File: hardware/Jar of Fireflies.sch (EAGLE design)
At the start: 31 parts, among them IC1 ATTINY85, J1 PJ-006A, J3 SENSOR, J4 ICSP

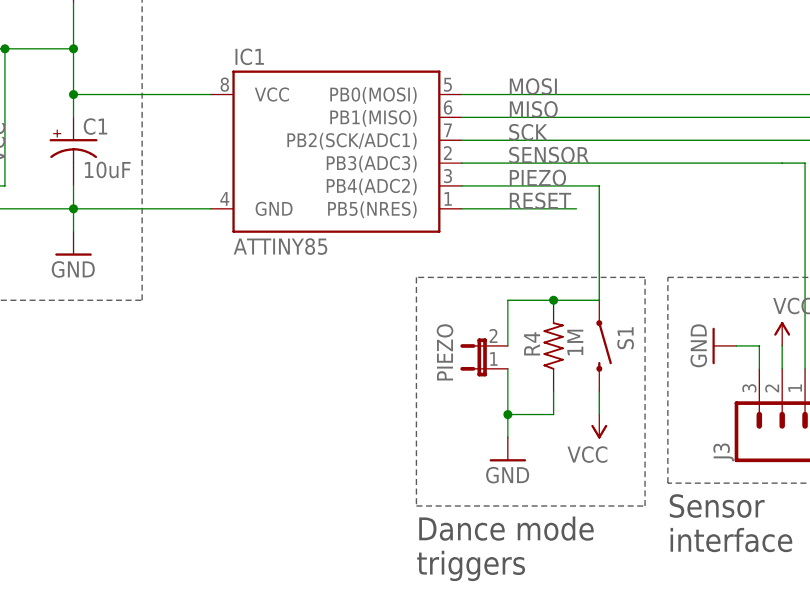
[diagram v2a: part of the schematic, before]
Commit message: Replacing pushbutton with sourced one
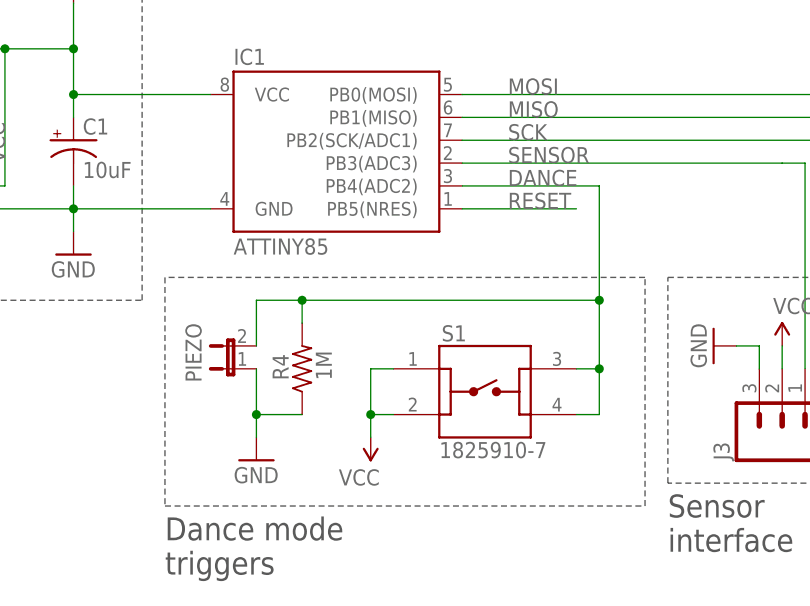
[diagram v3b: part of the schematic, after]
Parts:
- S1: value SWITCH-MOMENTARY-2PTH -> 1825910-7; device SparkFun-Electromechanical:SWITCH-MOMENTARY-2PTH -> 1825910-7:1825910-7
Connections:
- removed net N$2: PIEZO.2, R4.2, S1.1
- removed net PIEZO: IC1.PB4(ADC2)
- new net DANCE: IC1.PB4(ADC2), PIEZO.2, R4.2, S1.3, S1.4
- net VCC: now also S1.1
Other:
- moved on the sheet: PIEZO, R4
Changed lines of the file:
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@@
 <part name="GND2" library="supply1" deviceset="GND" device=""/>
 <part name="C1" library="SparkFun-Capacitors" deviceset="CAP_POL" device="PTH2" value="10uF"/>
-<part name="S1" library="SparkFun-Electromechanical" deviceset="SWITCH-MOMENTARY-2" device="PTH" value=""/>
 <part name="PAD1" library="wirepad" deviceset="SMD2" device=""/>
 <part name="PAD2" library="wirepad" deviceset="SMD2" device=""/>
@@
 <part name="J1" library="PJ-006A" deviceset="PJ-006A" device=""/>
 <part name="J2" library="SparkFun-Connectors" deviceset="M02" device="JST-PTH-VERT"/>
+<part name="S1" library="1825910-7" deviceset="1825910-7" device=""/>
 </parts>
 <sheets>
@@
 <wire x1="231.14" y1="78.74" x2="231.14" y2="124.46" width="0.1524" layer="97" style="longdash"/>
 <wire x1="231.14" y1="124.46" x2="142.24" y2="124.46" width="0.1524" layer="97" style="longdash"/>
-<wire x1="88.9" y1="99.06" x2="88.9" y2="73.66" width="0.1524" layer="97" style="longdash"/>
-<wire x1="88.9" y1="73.66" x2="114.3" y2="73.66" width="0.1524" layer="97" style="longdash"/>
+<wire x1="60.96" y1="99.06" x2="60.96" y2="73.66" width="0.1524" layer="97" style="longdash"/>
+<wire x1="60.96" y1="73.66" x2="114.3" y2="73.66" width="0.1524" layer="97" style="longdash"/>
 <wire x1="114.3" y1="73.66" x2="114.3" y2="99.06" width="0.1524" layer="97" style="longdash"/>
-<wire x1="114.3" y1="99.06" x2="88.9" y2="99.06" width="0.1524" layer="97" style="longdash"/>
+<wire x1="114.3" y1="99.06" x2="60.96" y2="99.06" width="0.1524" layer="97" style="longdash"/>
 <text x="20.32" y="139.7" size="2.54" layer="97" font="vector" ratio="15">Power</text>
-<text x="88.9" y="66.04" size="2.54" layer="97" font="vector" ratio="15">Dance mode
+<text x="60.96" y="66.04" size="2.54" layer="97" font="vector" ratio="15">Dance mode
 triggers</text>
 <text x="116.84" y="68.58" size="2.54" layer="97" font="vector" ratio="15">Sensor
@@
 </instance>
 <instance part="GND1" gate="1" x="50.8" y="101.6"/>
-<instance part="PIEZO" gate="A" x="96.52" y="88.9" smashed="yes" rot="R90">
-<attribute name="NAME" x="91.186" y="93.98" size="1.778" layer="95" rot="R270"/>
-<attribute name="VALUE" x="96.52" y="94.615" size="1.778" layer="96" rot="R180"/>
-</instance>
-<instance part="R4" gate="G$1" x="104.14" y="91.44" smashed="yes" rot="R90">
-<attribute name="NAME" x="102.6414" y="90.17" size="1.778" layer="95" rot="R90"/>
-<attribute name="VALUE" x="107.442" y="90.17" size="1.778" layer="96" rot="R90"/>
+<instance part="PIEZO" gate="A" x="68.58" y="88.9" smashed="yes" rot="R90">
+<attribute name="NAME" x="63.246" y="93.98" size="1.778" layer="95" rot="R270"/>
+<attribute name="VALUE" x="68.58" y="94.615" size="1.778" layer="96" rot="R180"/>
+</instance>
+<instance part="R4" gate="G$1" x="76.2" y="88.9" smashed="yes" rot="R90">
+<attribute name="NAME" x="74.7014" y="87.63" size="1.778" layer="95" rot="R90"/>
+<attribute name="VALUE" x="79.502" y="87.63" size="1.778" layer="96" rot="R90"/>
 </instance>
 <instance part="P+1" gate="1" x="50.8" y="129.54"/>
@@
 <attribute name="VALUE" x="153.67" y="80.518" size="1.778" layer="96"/>
 </instance>
-<instance part="GND2" gate="1" x="99.06" y="78.74"/>
+<instance part="GND2" gate="1" x="71.12" y="78.74"/>
 <instance part="C1" gate="G$1" x="50.8" y="114.3"/>
-<instance part="S1" gate="G$1" x="109.22" y="91.44" smashed="yes" rot="R270">
-<attribute name="NAME" x="111.252" y="93.726" size="1.778" layer="95" rot="R270"/>
-<attribute name="VALUE" x="106.68" y="93.98" size="1.778" layer="96" rot="R270"/>
-</instance>
 <instance part="PAD1" gate="1" x="165.1" y="111.76" smashed="yes" rot="R90">
 <attribute name="VALUE" x="168.402" y="110.617" size="1.778" layer="96" rot="R90"/>
@@
 <attribute name="VALUE" x="217.678" y="100.203" size="1.778" layer="96" rot="R270"/>
 </instance>
-<instance part="P+2" gate="1" x="109.22" y="83.82" rot="R180"/>
+<instance part="P+2" gate="1" x="83.82" y="81.28" rot="R180"/>
 <instance part="J4" gate="G$1" x="223.52" y="162.56"/>
 <instance part="P+3" gate="1" x="236.22" y="167.64"/>
@@
 <instance part="J1" gate="G$1" x="33.02" y="121.92"/>
 <instance part="J2" gate="G$1" x="30.48" y="106.68"/>
+<instance part="S1" gate="G$1" x="96.52" y="86.36"/>
 </instances>
 <busses>
@@
 </segment>
 <segment>
-<wire x1="99.06" y1="88.9" x2="99.06" y2="83.82" width="0.1524" layer="91"/>
-<wire x1="99.06" y1="83.82" x2="99.06" y2="81.28" width="0.1524" layer="91"/>
-<wire x1="104.14" y1="86.36" x2="104.14" y2="83.82" width="0.1524" layer="91"/>
-<wire x1="104.14" y1="83.82" x2="99.06" y2="83.82" width="0.1524" layer="91"/>
-<junction x="99.06" y="83.82"/>
+<wire x1="71.12" y1="88.9" x2="71.12" y2="83.82" width="0.1524" layer="91"/>
+<wire x1="71.12" y1="83.82" x2="71.12" y2="81.28" width="0.1524" layer="91"/>
+<wire x1="76.2" y1="83.82" x2="71.12" y2="83.82" width="0.1524" layer="91"/>
+<junction x="71.12" y="83.82"/>
 <pinref part="PIEZO" gate="A" pin="1"/>
 <pinref part="R4" gate="G$1" pin="1"/>
@@
 </segment>
 <segment>
-<pinref part="S1" gate="G$1" pin="2"/>
-<pinref part="P+2" gate="1" pin="VCC"/>
-<wire x1="109.22" y1="86.36" x2="109.22" y2="83.82" width="0.1524" layer="91"/>
-</segment>
-<segment>
 <pinref part="J4" gate="G$1" pin="2"/>
 <pinref part="P+3" gate="1" pin="VCC"/>
@@
 <pinref part="P+5" gate="1" pin="VCC"/>
 <wire x1="129.54" y1="88.9" x2="129.54" y2="91.44" width="0.1524" layer="91"/>
+</segment>
+<segment>
+<pinref part="S1" gate="G$1" pin="1"/>
+<pinref part="P+2" gate="1" pin="VCC"/>
+<wire x1="86.36" y1="88.9" x2="83.82" y2="88.9" width="0.1524" layer="91"/>
+<wire x1="83.82" y1="88.9" x2="83.82" y2="83.82" width="0.1524" layer="91"/>
+<pinref part="S1" gate="G$1" pin="2"/>
+<wire x1="83.82" y1="83.82" x2="83.82" y2="81.28" width="0.1524" layer="91"/>
+<wire x1="86.36" y1="83.82" x2="83.82" y2="83.82" width="0.1524" layer="91"/>
+<junction x="83.82" y="83.82"/>
 </segment>
 </net>
@@
 </segment>
 </net>
-<net name="PIEZO" class="0">
+<net name="DANCE" class="0">
 <segment>
 <wire x1="93.98" y1="109.22" x2="109.22" y2="109.22" width="0.1524" layer="91"/>
@@
 <pinref part="IC1" gate="G$1" pin="PB4(ADC2)"/>
 <wire x1="109.22" y1="109.22" x2="109.22" y2="96.52" width="0.1524" layer="91"/>
+<pinref part="S1" gate="G$1" pin="4"/>
+<wire x1="106.68" y1="83.82" x2="109.22" y2="83.82" width="0.1524" layer="91"/>
+<wire x1="109.22" y1="83.82" x2="109.22" y2="88.9" width="0.1524" layer="91"/>
+<pinref part="S1" gate="G$1" pin="3"/>
+<wire x1="109.22" y1="88.9" x2="109.22" y2="96.52" width="0.1524" layer="91"/>
+<wire x1="106.68" y1="88.9" x2="109.22" y2="88.9" width="0.1524" layer="91"/>
+<junction x="109.22" y="88.9"/>
+<wire x1="71.12" y1="91.44" x2="71.12" y2="96.52" width="0.1524" layer="91"/>
+<pinref part="PIEZO" gate="A" pin="2"/>
+<wire x1="71.12" y1="96.52" x2="76.2" y2="96.52" width="0.1524" layer="91"/>
+<junction x="109.22" y="96.52"/>
+<pinref part="R4" gate="G$1" pin="2"/>
+<wire x1="76.2" y1="96.52" x2="109.22" y2="96.52" width="0.1524" layer="91"/>
+<wire x1="76.2" y1="93.98" x2="76.2" y2="96.52" width="0.1524" layer="91"/>
+<junction x="76.2" y="96.52"/>
 </segment>
 </net>
@@
 </segment>
 </net>
-<net name="N$2" class="0">
-<segment>
-<pinref part="R4" gate="G$1" pin="2"/>
-<pinref part="S1" gate="G$1" pin="1"/>
-<wire x1="109.22" y1="96.52" x2="104.14" y2="96.52" width="0.1524" layer="91"/>
-<junction x="104.14" y="96.52"/>
-<wire x1="104.14" y1="96.52" x2="99.06" y2="96.52" width="0.1524" layer="91"/>
-<wire x1="99.06" y1="91.44" x2="99.06" y2="96.52" width="0.1524" layer="91"/>
-<pinref part="PIEZO" gate="A" pin="2"/>
-</segment>
-</net>

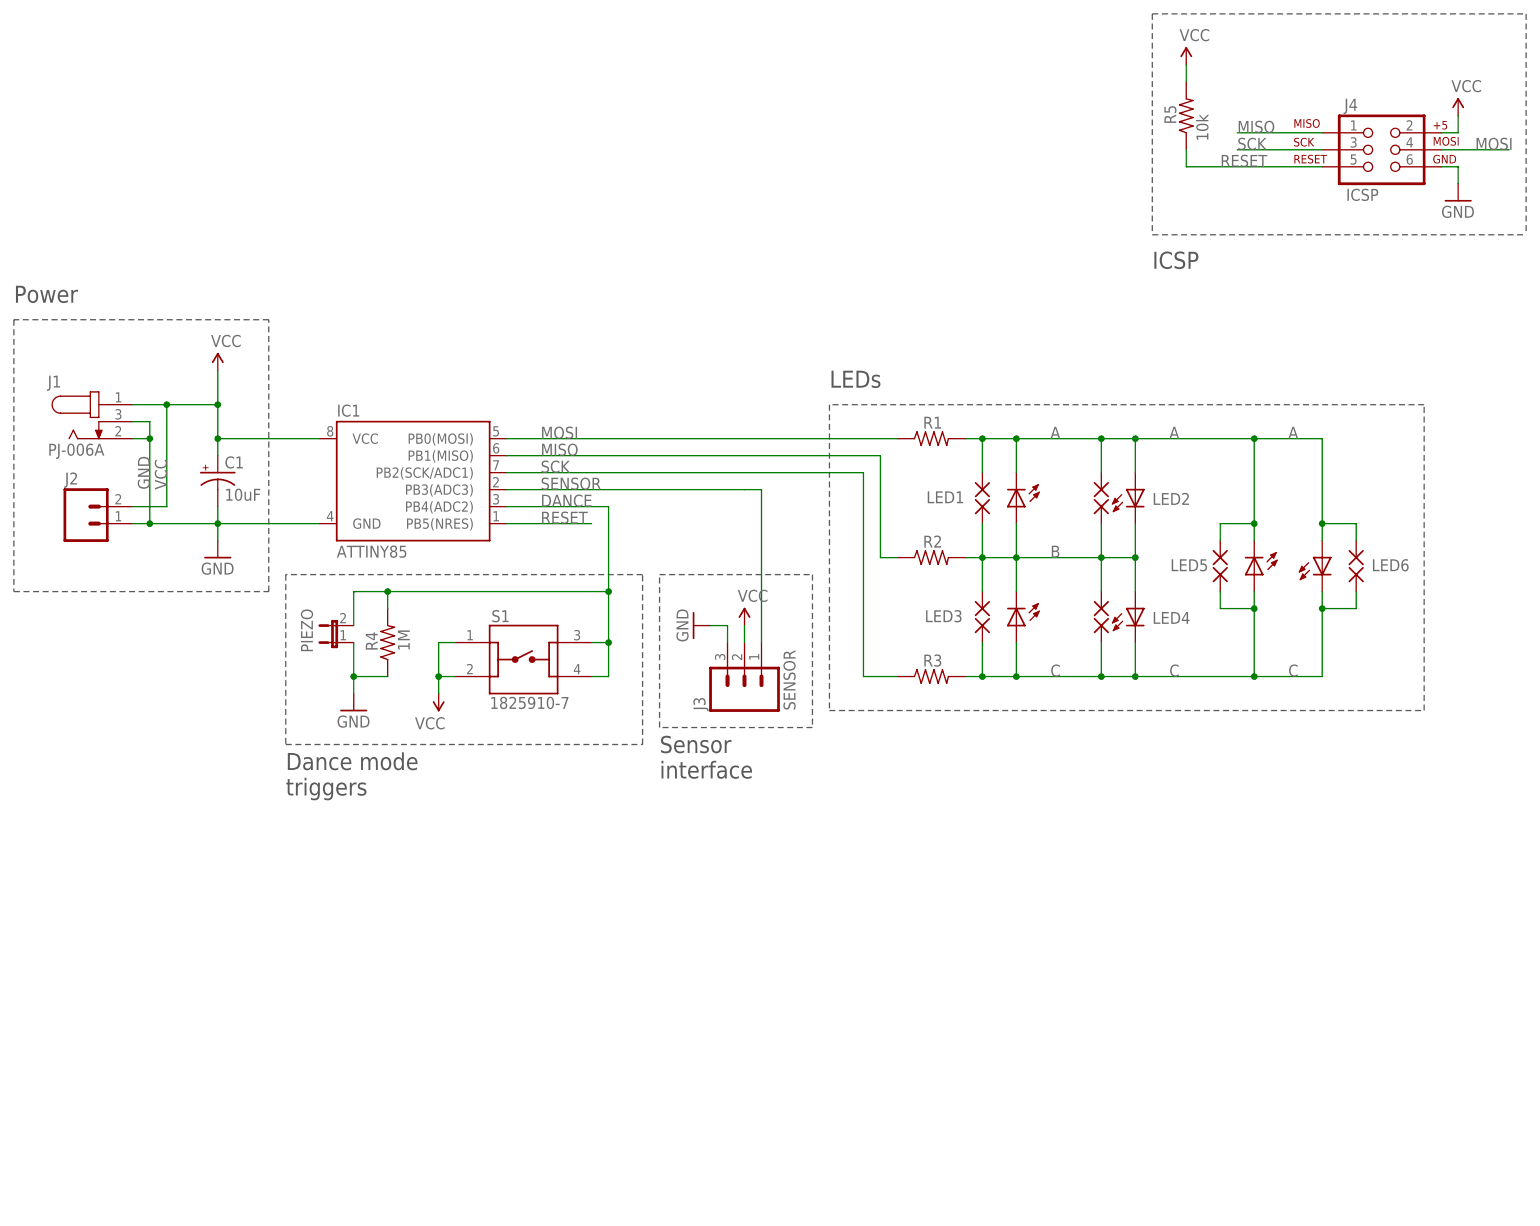
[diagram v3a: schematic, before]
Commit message: Removing piezo from PCB, making button switch to GND, adding solder pads to sensor interface
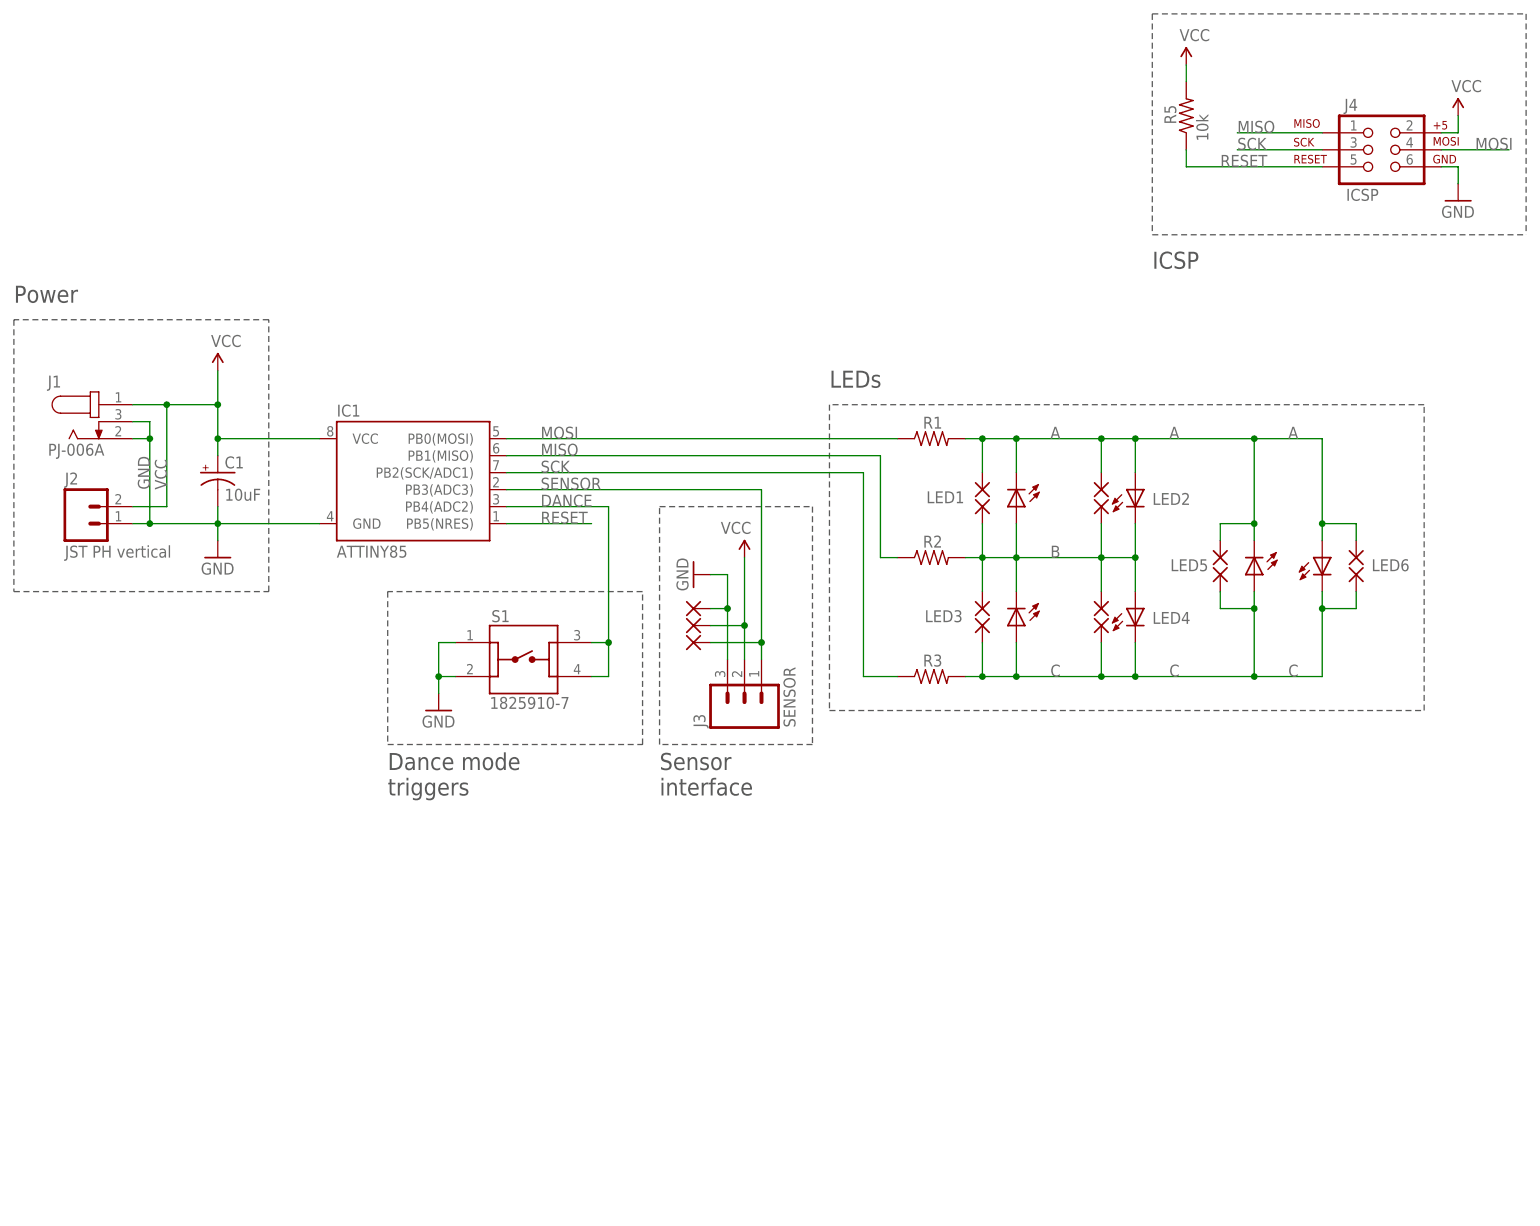
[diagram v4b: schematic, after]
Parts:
- removed PIEZO: (no value), SparkFun:JUMPER-2PTH
- removed R4: 1M, resistor:R-US_0204/7
- added PAD13, PAD14, PAD15: WIREPADSMD1,27-254, wirepad:WIREPADSMD1,27-254
- J2: value (none) -> JST PH vertical
- LED1, LED2, LED3, LED4, LED5, LED6: value (none) -> Amber
- R1, R2, R3: value (none) -> 150
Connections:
- net DANCE: no longer PIEZO.2, R4.2
- net GND: now also PAD13.P, S1.1, S1.2; no longer PIEZO.1, R4.1
- net SENSOR: now also PAD15.P
- net VCC: now also PAD14.P; no longer S1.1, S1.2
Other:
- moved on the sheet: J3
